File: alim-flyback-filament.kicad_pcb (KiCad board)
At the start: 2 copper layers, 90 x 70 mm, 87 parts, among them J1 HV80_IN, Q1 IPD050N10N5, Q2 IPD050N10N5, Q3 BSS127I, Q4 MMBT2222, Q5 BSS127I, T1 MSD1514-103ME, U1 UCC27517, U10 ISO7710, U11 AMC0311R, U12 UCC24612, U3 ISO7710, U5 DPC817, U7 AMC0311R, U8 AMC0311R, U9 AMC0302R

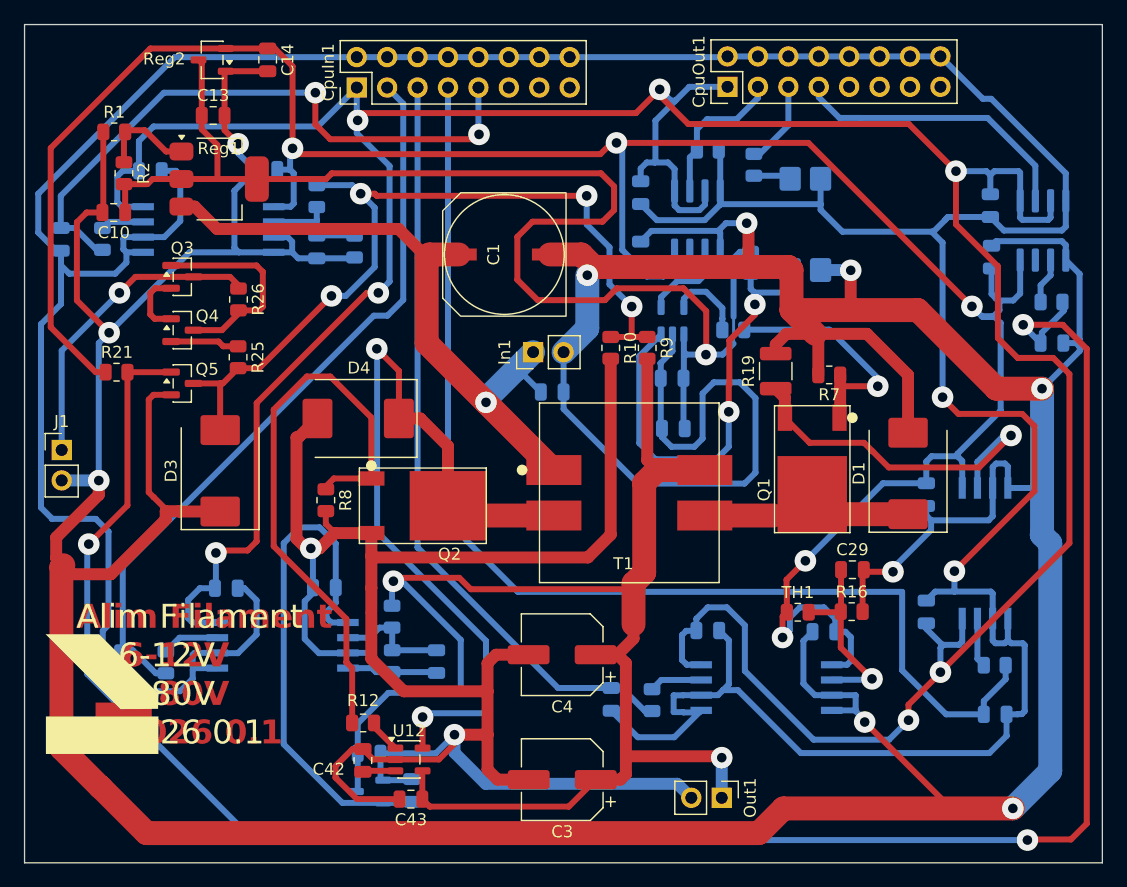
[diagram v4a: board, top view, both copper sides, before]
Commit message: Mise a jour routage PCB, resultats de simulation, et renommage du depot devkit
alim-flyback-filament.kicad_pcb : progression du routage. Nouveaux
resultats de simulation (clamp SMCJ43A/54A, comparaison Schottky,
enveloppe eta/Vds). 00-intention-conception.md : reference au depot
devkit renomme (shield-c2000 -> KICAD-C2000-devkit).

Co-Authored-By: Claude Sonnet 5 <noreply@anthropic.com>
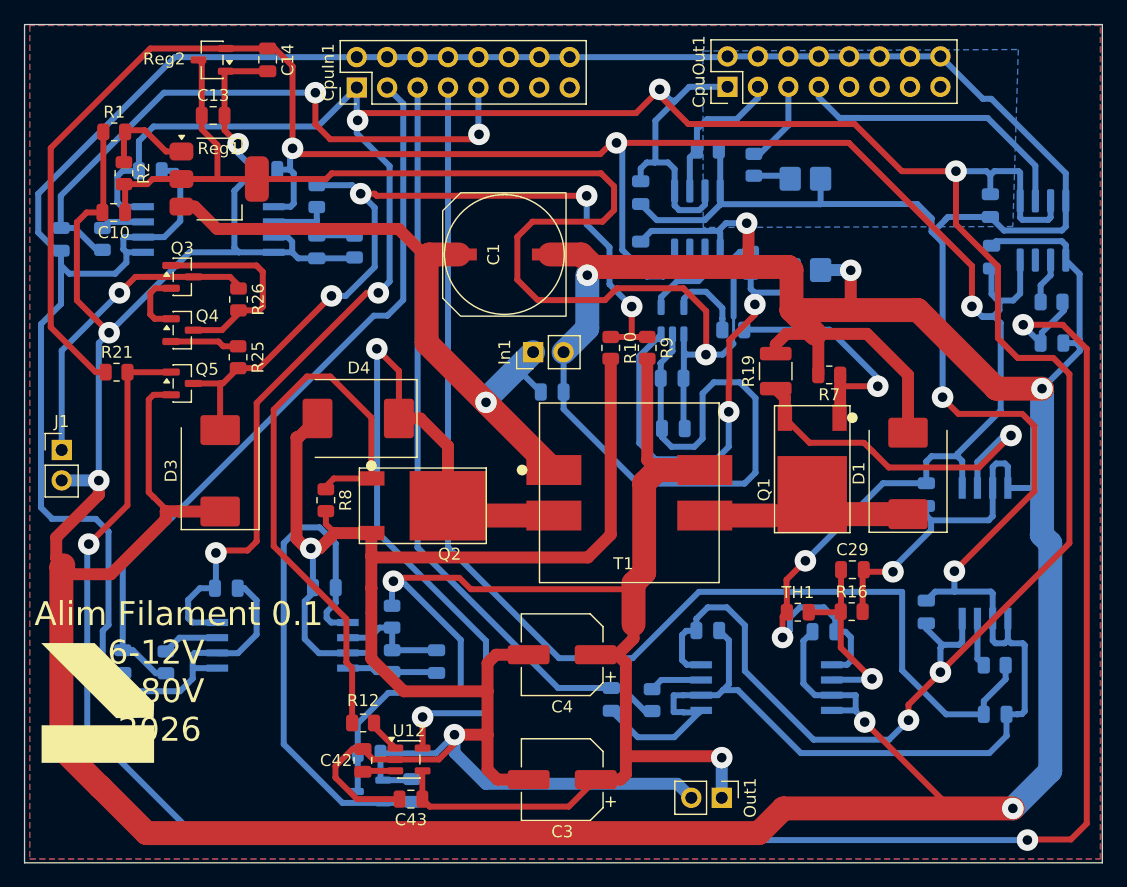
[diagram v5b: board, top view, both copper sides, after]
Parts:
- removed the ? at (34.4, 76.4)
- moved ? 0.83 mm to (32.4, 77.4)
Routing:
- net ISENSE_PRI_FBACK: track 96.4 -> 102.2 mm
- net VAR_GATE: track 173.0 -> 175.6 mm
- net RAIL_3V3_PRI: track 205.1 -> 207.1 mm
- added copper zone on B.Cu, net GND
- added copper zone on F.Cu, net GND
- added copper zone on B.Cu, net GND_CTRL
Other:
- board text added: "Alim Filament 0.1 6-12V 0-80V 2026"
- board text removed: "Alim Filament 6-12V 0-80V 2026 0.1"
